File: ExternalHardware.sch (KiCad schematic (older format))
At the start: 16 parts

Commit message: link up pre-existing external hardware
Fix errors and make sure we are using AHC parts
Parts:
- removed C?: 0.1uF, Capacitor_SMD:C_0805_2012Metric_Pad1.18x1.45mm_HandSolder, symbol Device:C
- removed U?: 74LVC1G79, Package_TO_SOT_SMD:SOT-23-5_HandSoldering, symbol 74xGxx:74LVC1G79
- added C17: 0.1uF, Capacitor_SMD:C_0805_2012Metric_Pad1.18x1.45mm_HandSolder, symbol Device:C
- added R6: 10k, Resistor_SMD:R_0805_2012Metric_Pad1.20x1.40mm_HandSolder, symbol Device:R
- added U7: 74AHC174, Package_SO:SOIC-16_3.9x9.9mm_P1.27mm, symbol 74xx:74LS174
- U6: renamed from U?; value 74LS04 -> 74AHC04; footprint Package_DIP:DIP-14_W7.62mm_Socket -> Package_SO:SOIC-14_3.9x8.7mm_P1.27mm
- U8: renamed from U?; value 74LS08 -> 74AHC08; footprint Package_DIP:DIP-14_W7.62mm_Socket -> Package_SO:SOIC-14_3.9x8.7mm_P1.27mm
- U9: renamed from U?; value 74LS174 -> 74AHC174; footprint Package_DIP:DIP-16_W7.62mm_Socket -> Package_SO:SOIC-16_3.9x9.9mm_P1.27mm
- gave numbers to parts that had none: 4
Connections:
- net labels added: ~MR1, ~READY960
- net labels removed: ~RDY
- wire segments 51 -> 55
- no-connect marks 6 -> 16
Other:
- moved on the sheet: C18, C20, U6A, U6B, U6D, U6F, U6G, U8A, U8B, U8C, U8E

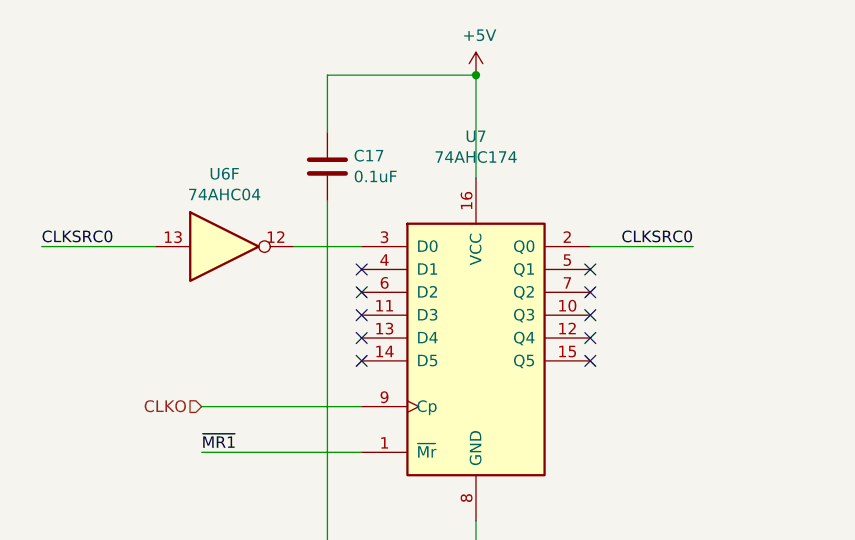
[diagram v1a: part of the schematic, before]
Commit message: Rearrange some connections and try to shove the aux hardware closer together
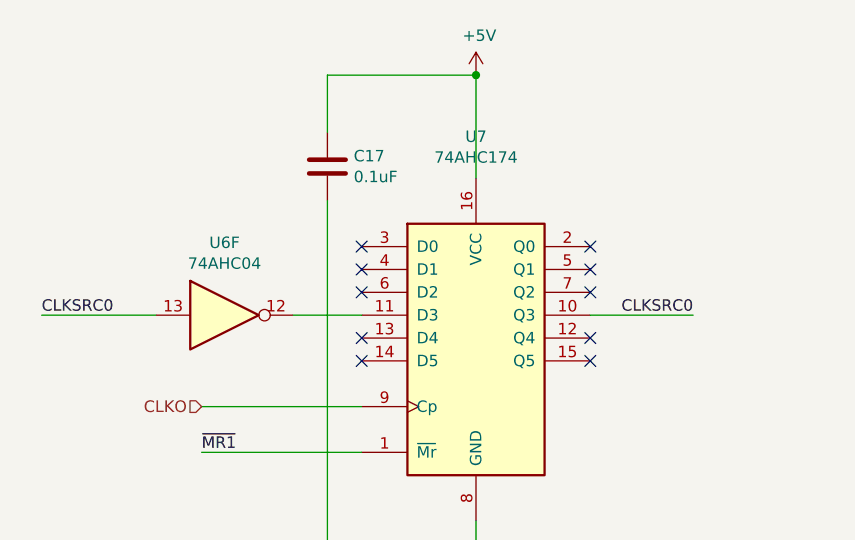
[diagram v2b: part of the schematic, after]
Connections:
- net CLKSRC0: now also U7.10 (Q3); no longer U7.2 (Q0)
- net at U7.11 (D3): now also U6.12
- net at U7.3 (D0): no longer U6.12
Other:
- moved on the sheet: U6F
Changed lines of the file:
@@
 	2150 7150 2700 7150
 Wire Wire Line
-	550  1500 1050 1500
-Text Label 550  1500 0    50   ~ 0
+	550  1800 1050 1800
+Text Label 550  1800 0    50   ~ 0
 CLKSRC0
 Text Notes 3250 4150 0    118  ~ 0
@@
 L 74xx:74LS04 U?
 U 6 1 6CB975FD
-P 1350 1500
+P 1350 1800
 AR Path="/6CB975FD" Ref="U?"  Part="6"
 AR Path="/6CB8E383/6CB975FD" Ref="U?"  Part="6"
 AR Path="/62305776/6CB975FD" Ref="U6"  Part="6"
-F 0 "U6" H 1350 1817 50  0000 C CNN
-F 1 "74AHC04" H 1350 1726 50  0000 C CNN
-F 2 "Package_SO:SOIC-14_3.9x8.7mm_P1.27mm" H 1350 1500 50  0001 C CNN
-F 3 "http://www.ti.com/lit/gpn/sn74LS04" H 1350 1500 50  0001 C CNN
-	6    1350 1500
-	1    0    0    -1
-$EndComp
-Text Label 3400 1500 2    50   ~ 0
+F 0 "U6" H 1350 2117 50  0000 C CNN
+F 1 "74AHC04" H 1350 2026 50  0000 C CNN
+F 2 "Package_SO:SOIC-14_3.9x8.7mm_P1.27mm" H 1350 1800 50  0001 C CNN
+F 3 "http://www.ti.com/lit/gpn/sn74LS04" H 1350 1800 50  0001 C CNN
+	6    1350 1800
+	1    0    0    -1
+$EndComp
+Text Label 3400 1800 2    50   ~ 0
 CLKSRC0
 $Comp
@@
 Connection ~ 2450 2900
 Wire Wire Line
-	2950 1500 3400 1500
+	2950 1800 3400 1800
 NoConn ~ 2950 1900
 NoConn ~ 1950 1900
 Wire Wire Line
 	1950 2400 1250 2400
-NoConn ~ 1950 1800
-NoConn ~ 2950 1800
 NoConn ~ 1950 2000
 NoConn ~ 2950 2000
@@
 NoConn ~ 2950 1700
 Wire Wire Line
-	1650 1500 1950 1500
+	1650 1800 1950 1800
 Text HLabel 1300 5050 0    50   Input ~ 0
 ~BLAST~\~FAIL~
@@
 Text HLabel 1300 5850 0    50   Input ~ 0
 ~BE0
+NoConn ~ 2950 1500
+NoConn ~ 1950 1500
 $EndSCHEMATC

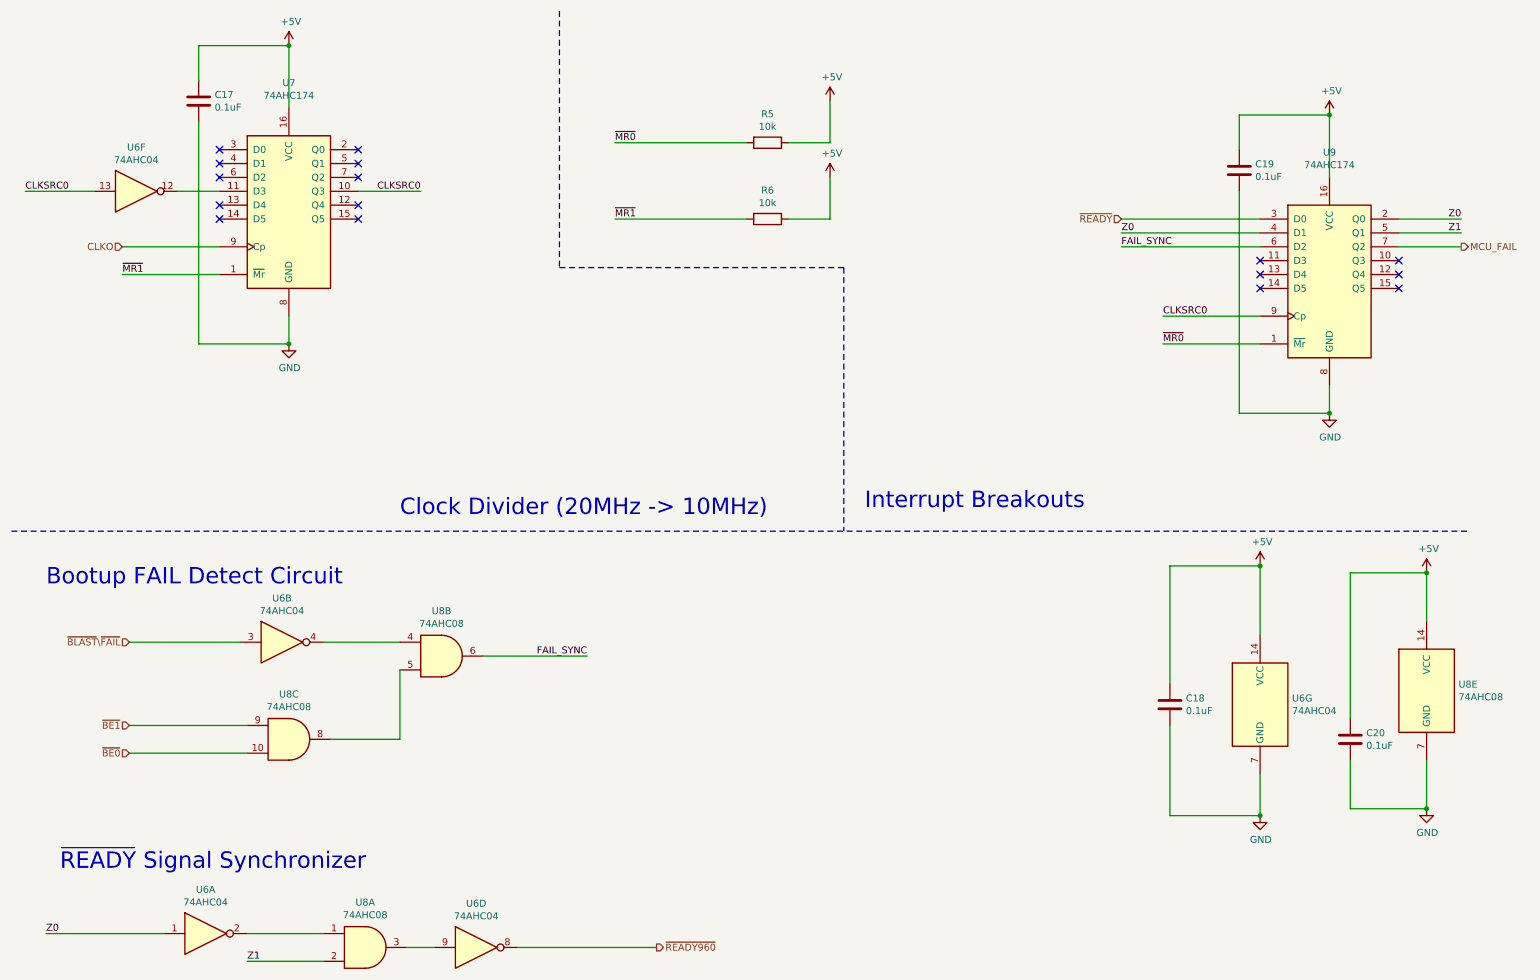
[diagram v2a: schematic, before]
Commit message: Rearrange aux hardware to reduce via count
Start routing the rest of the traces out of the i960
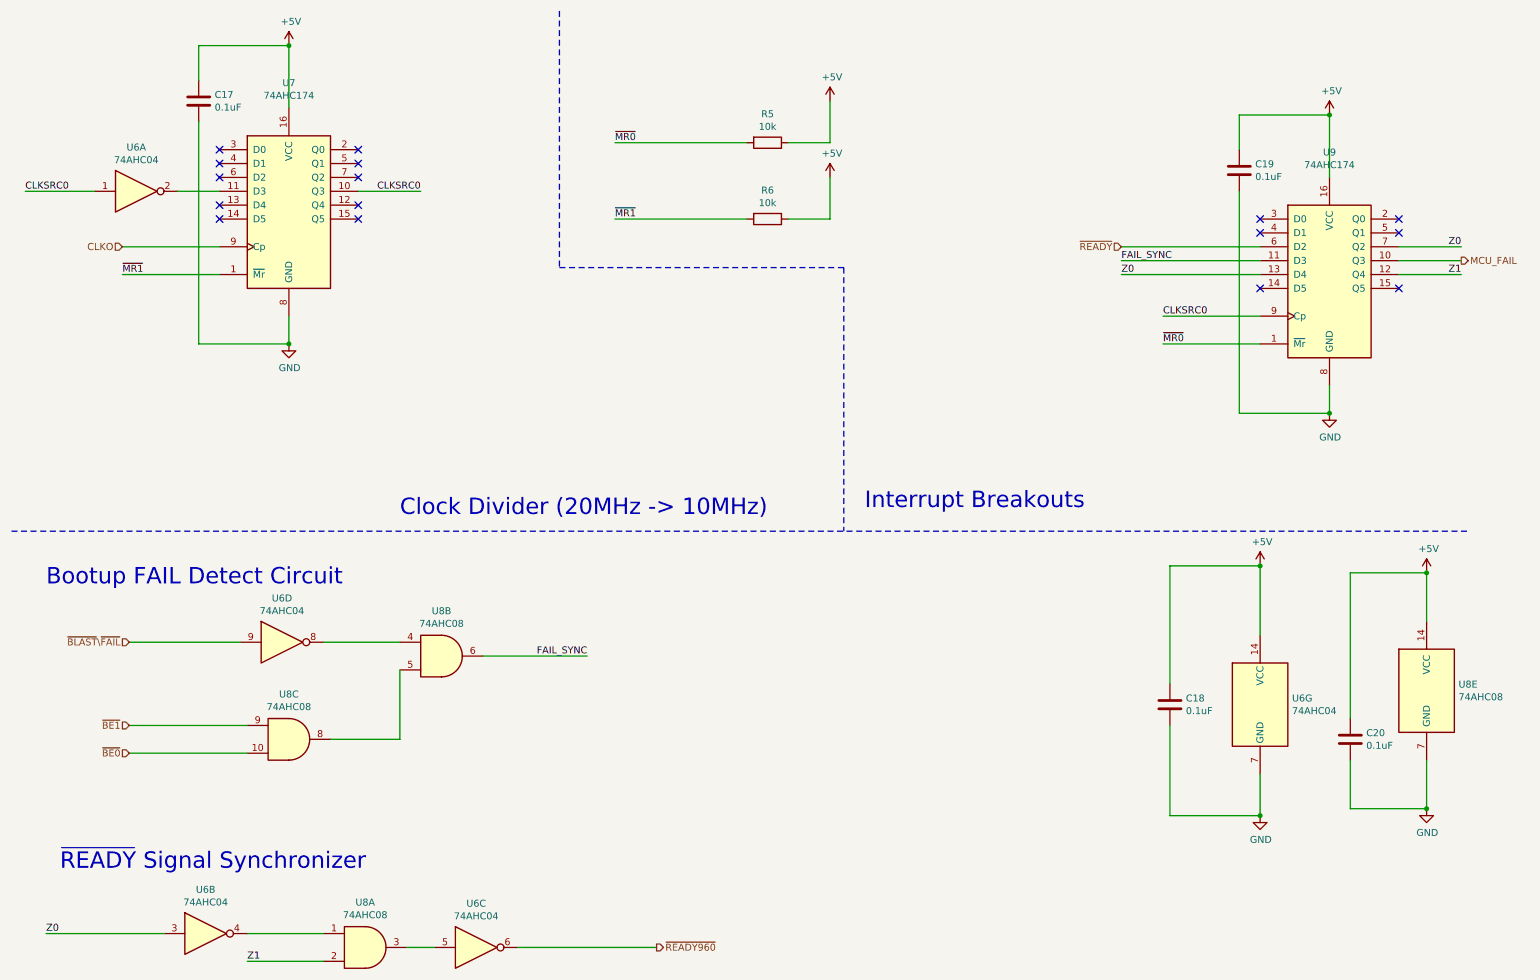
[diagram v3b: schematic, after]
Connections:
- net CLKSRC0: now also U6.1; no longer U6.13
- net FAIL_SYNC: now also U9.11 (D3); no longer U9.6 (D2)
- net MCU_FAIL: now also U9.10 (Q3); no longer U9.7 (Q2)
- net Z0: now also U6.3, U9.13 (D4), U9.7 (Q2); no longer U6.1, U9.2 (Q0), U9.4 (D1)
- net Z1: now also U9.12 (Q4); no longer U9.5 (Q1)
- net ~BLAST~\~FAIL~: now also U6.9; no longer U6.3
- net ~READY: now also U9.6 (D2); no longer U9.3 (D0)
- net ~READY960: now also U6.6; no longer U6.8
- net at U7.11 (D3): now also U6.2; no longer U6.12
- net at U8.1: now also U6.4; no longer U6.2
- net at U8.3: now also U6.5; no longer U6.9
- net at U8.4: now also U6.8; no longer U6.4
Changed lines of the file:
@@
 	4400 500  4400 2350
 Wire Wire Line
-	2150 7350 2700 7350
+	2150 7150 2700 7150
 Text Notes 800  6700 0    118  ~ 0
 ~READY~ Signal Synchronizer
@@
 $Comp
 L 74xx:74LS04 U?
-U 4 1 6CB975D6
+U 3 1 6CB975D6
 P 3800 7250
 AR Path="/60861C6D/6CB975D6" Ref="U?"  Part="4"
 AR Path="/6CB975D6" Ref="U?"  Part="4"
 AR Path="/6CB8E383/6CB975D6" Ref="U?"  Part="4"
-AR Path="/62305776/6CB975D6" Ref="U6"  Part="4"
+AR Path="/62305776/6CB975D6" Ref="U6"  Part="3"
 F 0 "U6" H 3800 7567 50  0000 C CNN
 F 1 "74AHC04" H 3800 7476 50  0000 C CNN
 F 2 "Package_SO:SOIC-14_3.9x8.7mm_P1.27mm" H 3800 7250 50  0001 C CNN
 F 3 "http://www.ti.com/lit/gpn/sn74LS04" H 3800 7250 50  0001 C CNN
-	4    3800 7250
+	3    3800 7250
 	1    0    0    -1
 $EndComp
@@
 	700  7150 1550 7150
 Wire Wire Line
-	2150 7150 2700 7150
+	2150 7350 2700 7350
 Wire Wire Line
 	550  1800 1050 1800
@@
 $Comp
 L 74xx:74LS04 U?
-U 6 1 6CB975FD
+U 1 1 6CB975FD
 P 1350 1800
 AR Path="/6CB975FD" Ref="U?"  Part="6"
 AR Path="/6CB8E383/6CB975FD" Ref="U?"  Part="6"
-AR Path="/62305776/6CB975FD" Ref="U6"  Part="6"
+AR Path="/62305776/6CB975FD" Ref="U6"  Part="1"
 F 0 "U6" H 1350 2117 50  0000 C CNN
 F 1 "74AHC04" H 1350 2026 50  0000 C CNN
 F 2 "Package_SO:SOIC-14_3.9x8.7mm_P1.27mm" H 1350 1800 50  0001 C CNN
 F 3 "http://www.ti.com/lit/gpn/sn74LS04" H 1350 1800 50  0001 C CNN
-	6    1350 1800
+	1    1350 1800
 	1    0    0    -1
 $EndComp
@@
 $Comp
 L 74xx:74LS04 U?
-U 2 1 6CB97620
+U 4 1 6CB97620
 P 2400 5050
 AR Path="/6CB97620" Ref="U?"  Part="2"
 AR Path="/6CB8E383/6CB97620" Ref="U?"  Part="2"
-AR Path="/62305776/6CB97620" Ref="U6"  Part="2"
+AR Path="/62305776/6CB97620" Ref="U6"  Part="4"
 F 0 "U6" H 2400 5367 50  0000 C CNN
 F 1 "74AHC04" H 2400 5276 50  0000 C CNN
 F 2 "Package_SO:SOIC-14_3.9x8.7mm_P1.27mm" H 2400 5050 50  0001 C CNN
 F 3 "http://www.ti.com/lit/gpn/sn74LS04" H 2400 5050 50  0001 C CNN
-	2    2400 5050
+	4    2400 5050
 	1    0    0    -1
 $EndComp
 $Comp
 L 74xx:74LS04 U?
-U 1 1 6CB97626
+U 2 1 6CB97626
 P 1850 7150
 AR Path="/6CB97626" Ref="U?"  Part="1"
 AR Path="/6CB8E383/6CB97626" Ref="U?"  Part="1"
-AR Path="/62305776/6CB97626" Ref="U6"  Part="1"
+AR Path="/62305776/6CB97626" Ref="U6"  Part="2"
 F 0 "U6" H 1850 7467 50  0000 C CNN
 F 1 "74AHC04" H 1850 7376 50  0000 C CNN
 F 2 "Package_SO:SOIC-14_3.9x8.7mm_P1.27mm" H 1850 7150 50  0001 C CNN
 F 3 "http://www.ti.com/lit/gpn/sn74LS04" H 1850 7150 50  0001 C CNN
-	1    1850 7150
+	2    1850 7150
 	1    0    0    -1
 $EndComp
@@
 Connection ~ 9950 3400
 Wire Wire Line
-	9450 2000 8450 2000
-Wire Wire Line
-	10450 2000 10900 2000
-Wire Wire Line
-	10450 2100 10900 2100
-NoConn ~ 10450 2400
-NoConn ~ 9450 2400
-Wire Wire Line
-	9450 2100 8450 2100
+	9450 2200 8450 2200
+Wire Wire Line
+	10450 2200 10900 2200
+Wire Wire Line
+	10450 2400 10900 2400
+Wire Wire Line
+	9450 2400 8450 2400
 Wire Wire Line
 	9450 2900 8750 2900
-Text Label 10900 2000 2    51   ~ 0
+Text Label 10900 2200 2    51   ~ 0
 Z0
-Text Label 8450 2100 0    51   ~ 0
+Text Label 8450 2400 0    51   ~ 0
 Z0
-Text Label 10900 2100 2    51   ~ 0
+Text Label 10900 2400 2    51   ~ 0
 Z1
 Text Label 8750 2900 0    50   ~ 0
 ~MR0
-NoConn ~ 9450 2300
-NoConn ~ 10450 2300
-NoConn ~ 9450 2500
-NoConn ~ 10450 2500
-Wire Wire Line
-	10900 2200 10450 2200
-Wire Wire Line
-	9450 2200 8450 2200
-Text Label 8450 2200 0    50   ~ 0
+Wire Wire Line
+	10900 2300 10450 2300
+Wire Wire Line
+	9450 2300 8450 2300
+Text Label 8450 2300 0    50   ~ 0
 FAIL_SYNC
 Text HLabel 5100 7250 2    50   Output ~ 0
 ~READY960
-Text HLabel 10900 2200 2    50   Output ~ 0
+Text HLabel 10900 2300 2    50   Output ~ 0
 MCU_FAIL
-Text HLabel 8450 2000 0    51   Input ~ 0
+Text HLabel 8450 2200 0    51   Input ~ 0
 ~READY
 Text Label 8750 2700 0    51   ~ 0
@@
 ~MR1
 NoConn ~ 1950 1600
-NoConn ~ 1950 1700
 NoConn ~ 2950 1600
-NoConn ~ 2950 1700
 Wire Wire Line
 	1650 1800 1950 1800
@@
 NoConn ~ 2950 1500
 NoConn ~ 1950 1500
+NoConn ~ 9450 2000
+NoConn ~ 9450 2100
+NoConn ~ 10450 2000
+NoConn ~ 10450 2100
+NoConn ~ 10450 2500
+NoConn ~ 9450 2500
+NoConn ~ 1950 1700
+NoConn ~ 2950 1700
 $EndSCHEMATC

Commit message: expose clock signal div 2
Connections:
- net CLKSRC0 renamed CLKDIV2
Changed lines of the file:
@@
 NoConn ~ 1950 1700
 NoConn ~ 2950 1700
+Text Label 4850 2850 0    50   ~ 0
+CLKSRC0
+Wire Wire Line
+	4850 2850 5550 2850
+Text HLabel 5550 2850 2    50   Output ~ 0
+CLKDIV2
 $EndSCHEMATC
